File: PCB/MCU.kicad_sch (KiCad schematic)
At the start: 36 parts, among them J1 MSD-1-A, SW33V1 Conn_01x01_Pin

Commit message: Updated component selection; Updated some footprints; Added .csv file in the export folder of the PCB that contains parts from DigiKey
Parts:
- Cnrst1: footprint Capacitor_SMD:C_0603_1608Metric -> Capacitor_SMD:C_0805_2012Metric
- Csd_shield1: footprint Capacitor_SMD:C_1206_3216Metric -> Capacitor_SMD:C_0805_2012Metric
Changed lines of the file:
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@@
 			)
 		)
-		(property "Footprint" "Capacitor_SMD:C_0603_1608Metric"
+		(property "Footprint" "Capacitor_SMD:C_0805_2012Metric"
 			(at 80.5688 32.766 0)
 			(effects
@@
 			)
 		)
-		(property "Footprint" "Capacitor_SMD:C_1206_3216Metric"
+		(property "Footprint" "Capacitor_SMD:C_0805_2012Metric"
 			(at 211.836 76.5048 0)
 			(effects

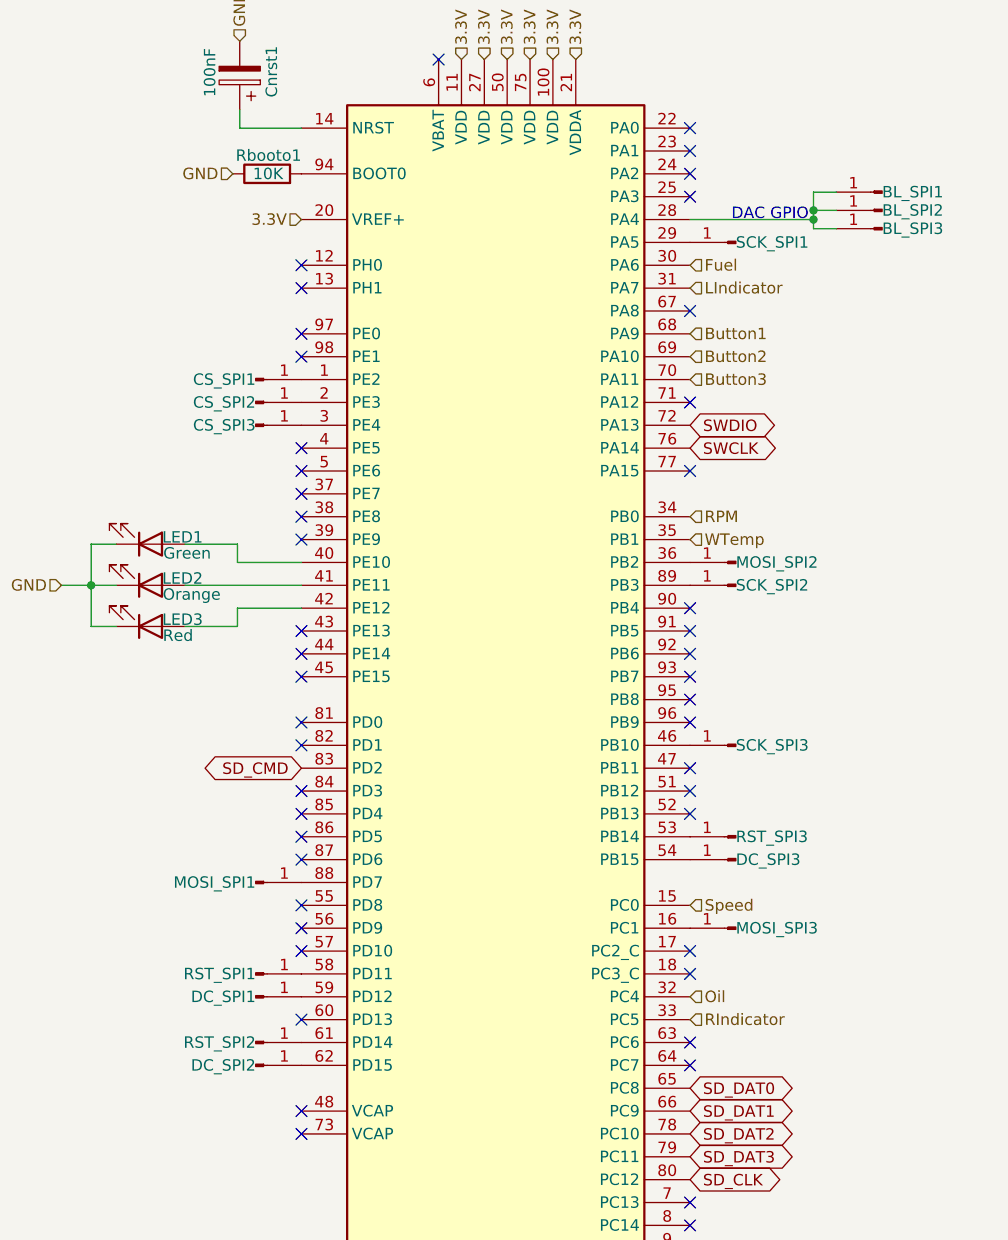
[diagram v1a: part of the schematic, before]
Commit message: Added 2x Temperature Sensors; Updated wrong GPIO connections in schematic; Set Button input GPIOs to Pull-Down; LED circuits need to be corrected
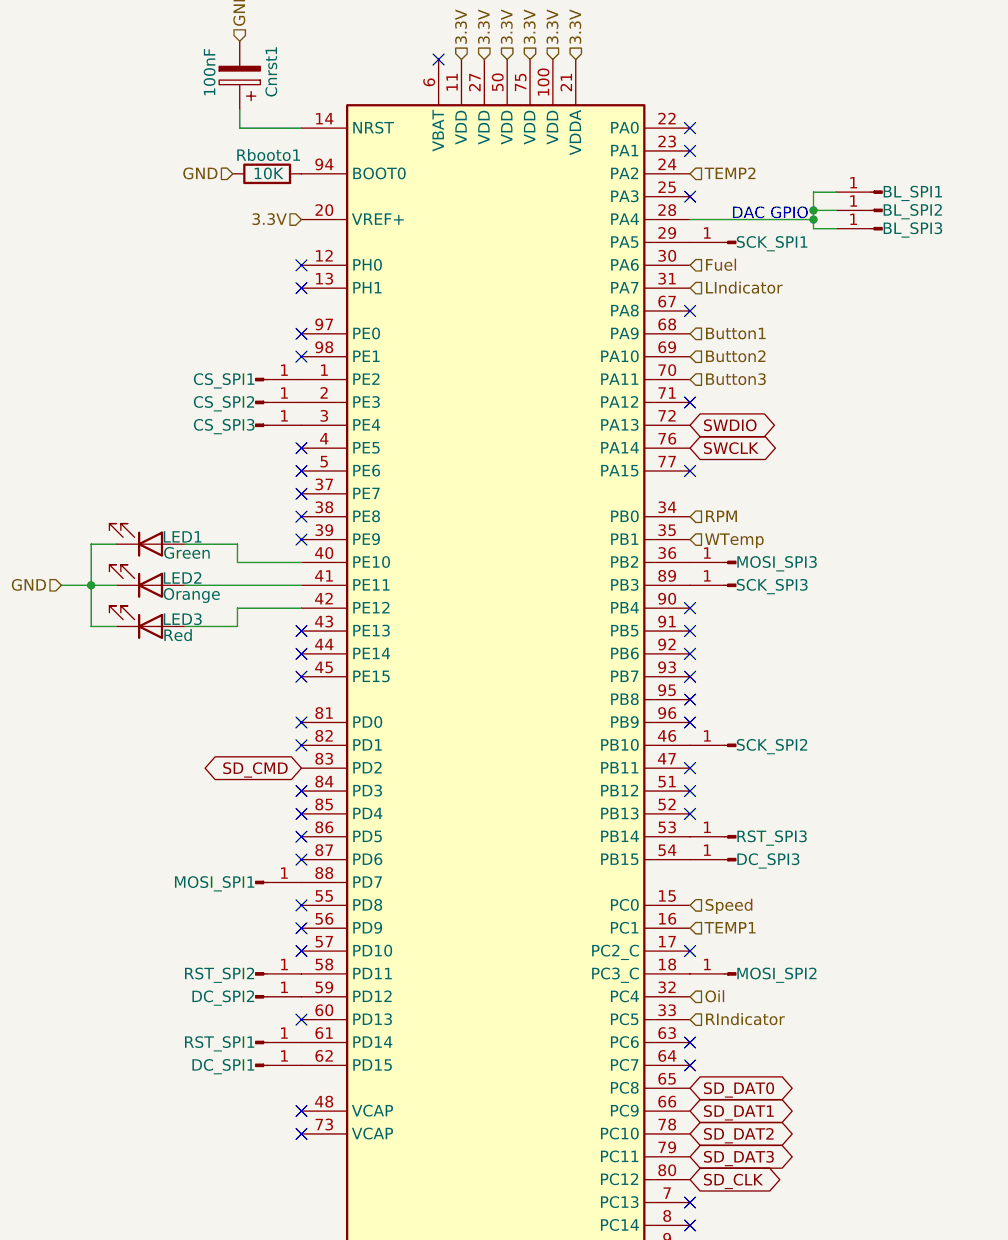
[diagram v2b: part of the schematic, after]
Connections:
- net at MOSI_SPI3.1 (Pin_1): now also STM1.36 (PB2); no longer STM1.16 (PC1)
- net at STM1.46 (PB10): now also SCK_SPI2.1 (Pin_1); no longer SCK_SPI3.1 (Pin_1)
- net at DC_SPI2.1 (Pin_1): now also STM1.59 (PD12); no longer STM1.62 (PD15)
- net at RST_SPI1.1 (Pin_1): now also STM1.61 (PD14); no longer STM1.58 (PD11)
- net at STM1.18 (PC3_C): now also MOSI_SPI2.1 (Pin_1)
- net TEMP2: now reaches STM1.24 (PA2)
- net at DC_SPI1.1 (Pin_1): now also STM1.62 (PD15); no longer STM1.59 (PD12)
- net at RST_SPI2.1 (Pin_1): now also STM1.58 (PD11); no longer STM1.61 (PD14)
- net at STM1.89 (PB3): now also SCK_SPI3.1 (Pin_1); no longer SCK_SPI2.1 (Pin_1)
- new net TEMP1: STM1.16 (PC1)
- no-connect marks 49 -> 47

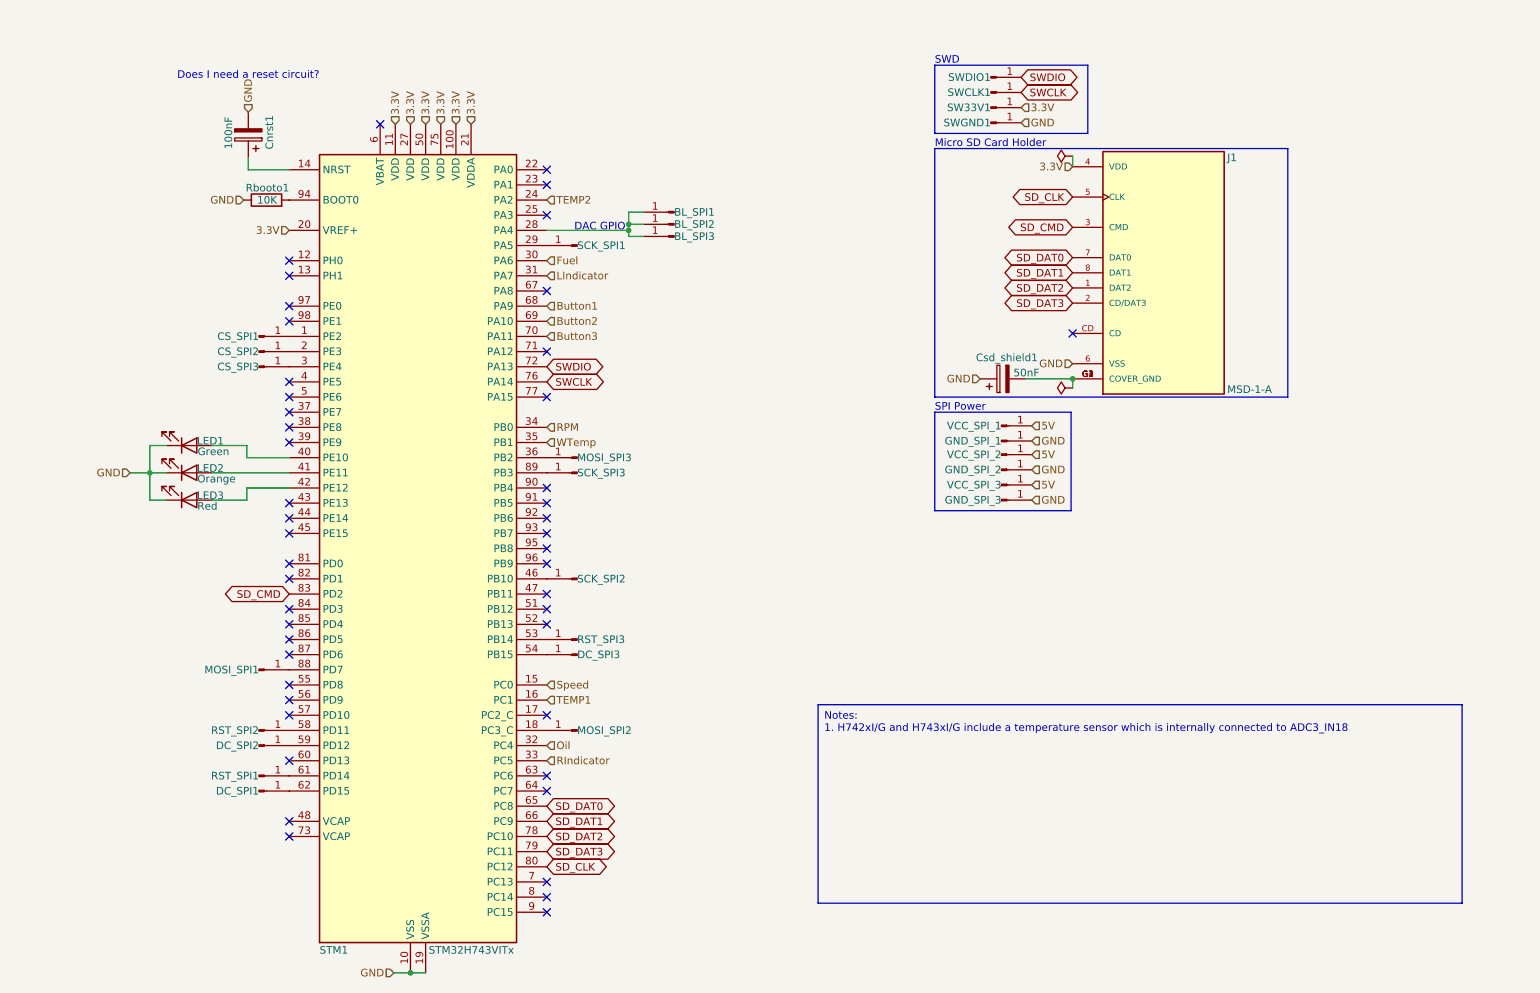
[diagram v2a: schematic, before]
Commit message: add resistors for status LEDs
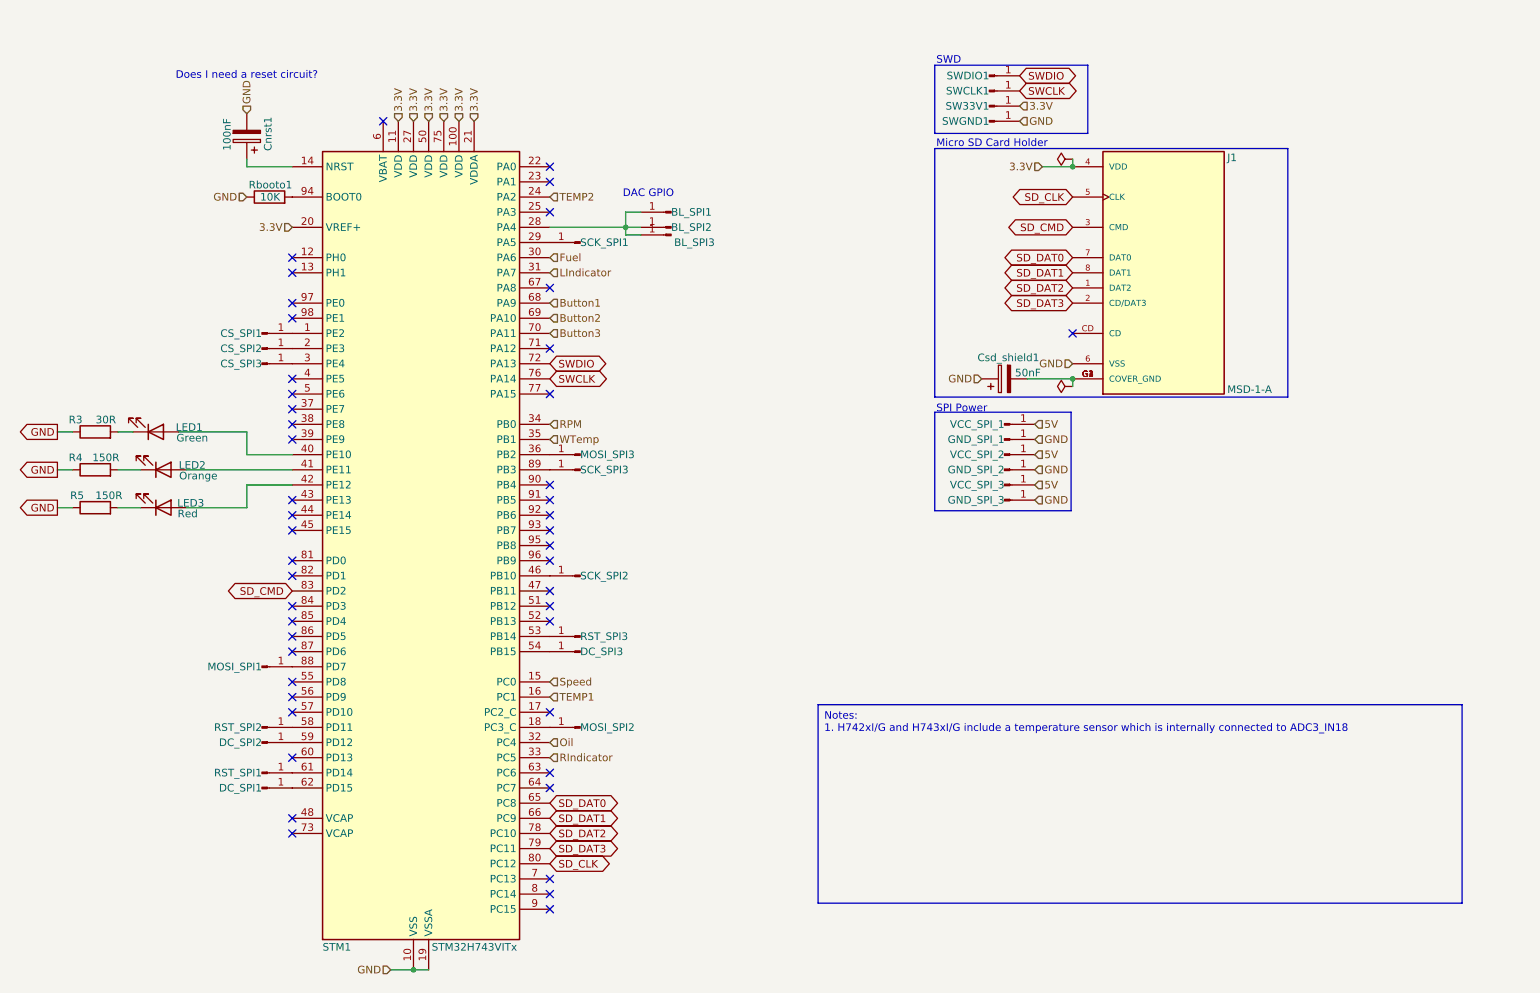
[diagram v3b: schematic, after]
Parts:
- added R3: 30R, symbol Device:R
- added R4, R5: 150R, symbol Device:R
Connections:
- net GND: now also R3.1, R4.1, R5.1; no longer LED1.1 (K), LED2.1 (K), LED3.1 (K)
- new net: LED2.1 (K), R4.2
- new net: LED1.1 (K), R3.2
- new net: LED3.1 (K), R5.2
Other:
- moved on the sheet: BL_SPI1, BL_SPI2, BL_SPI3, CS_SPI1, CS_SPI2, CS_SPI3, DC_SPI1, DC_SPI2, DC_SPI3, GND_SPI_1, GND_SPI_2, GND_SPI_3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

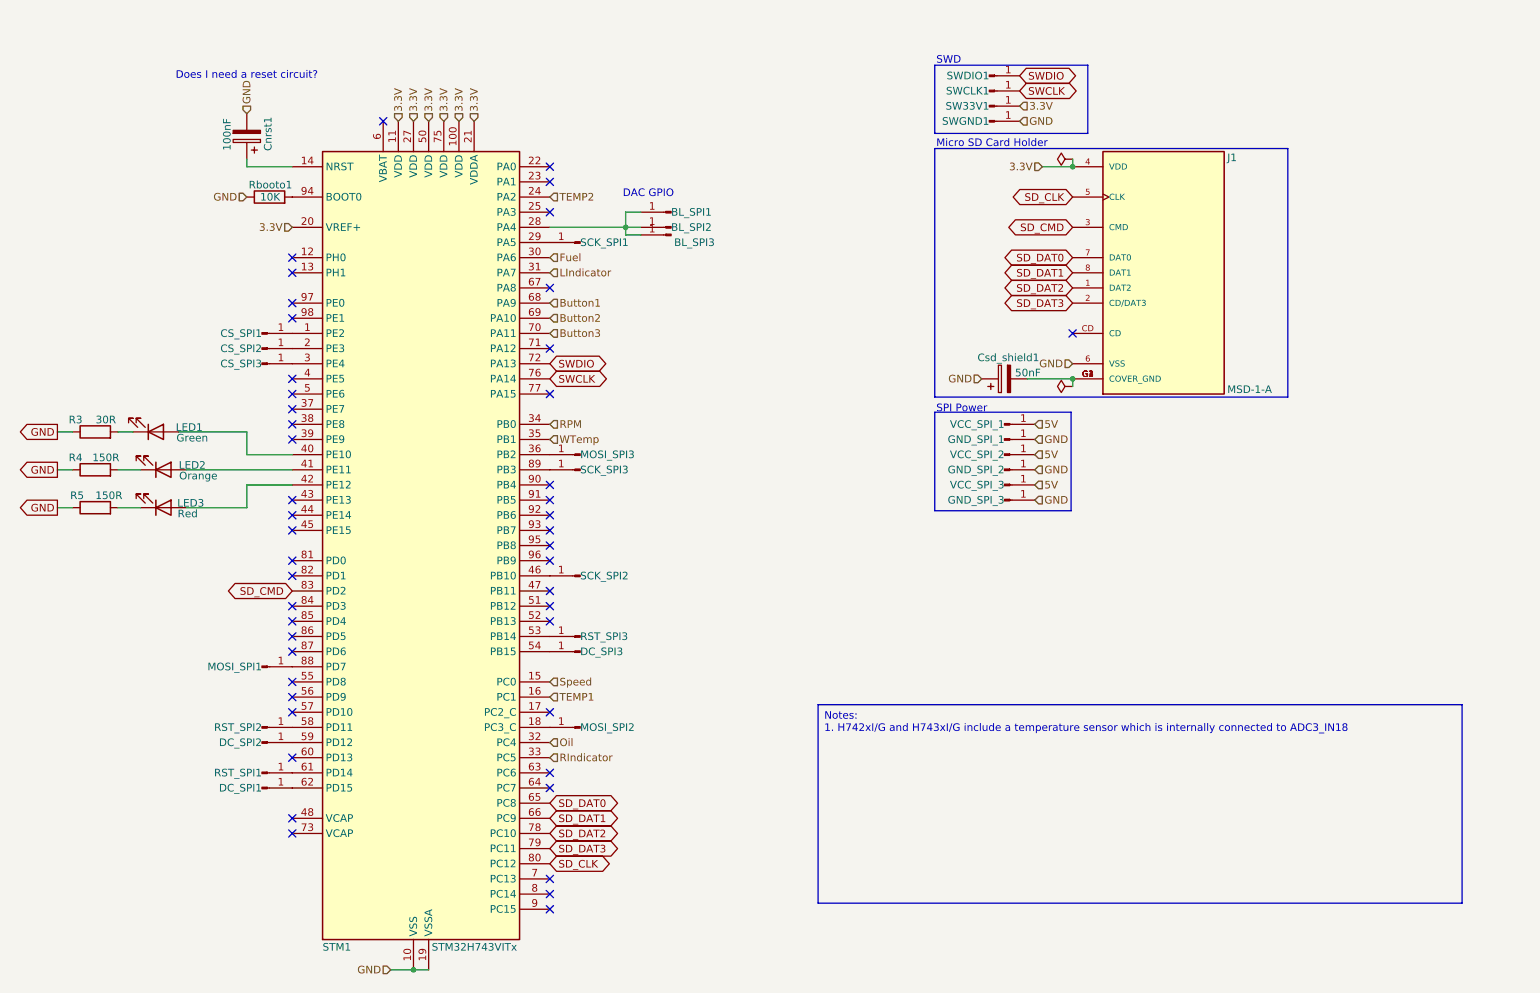
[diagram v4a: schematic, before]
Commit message: Replaced some global labels with power net(s); Added warning label for missing component
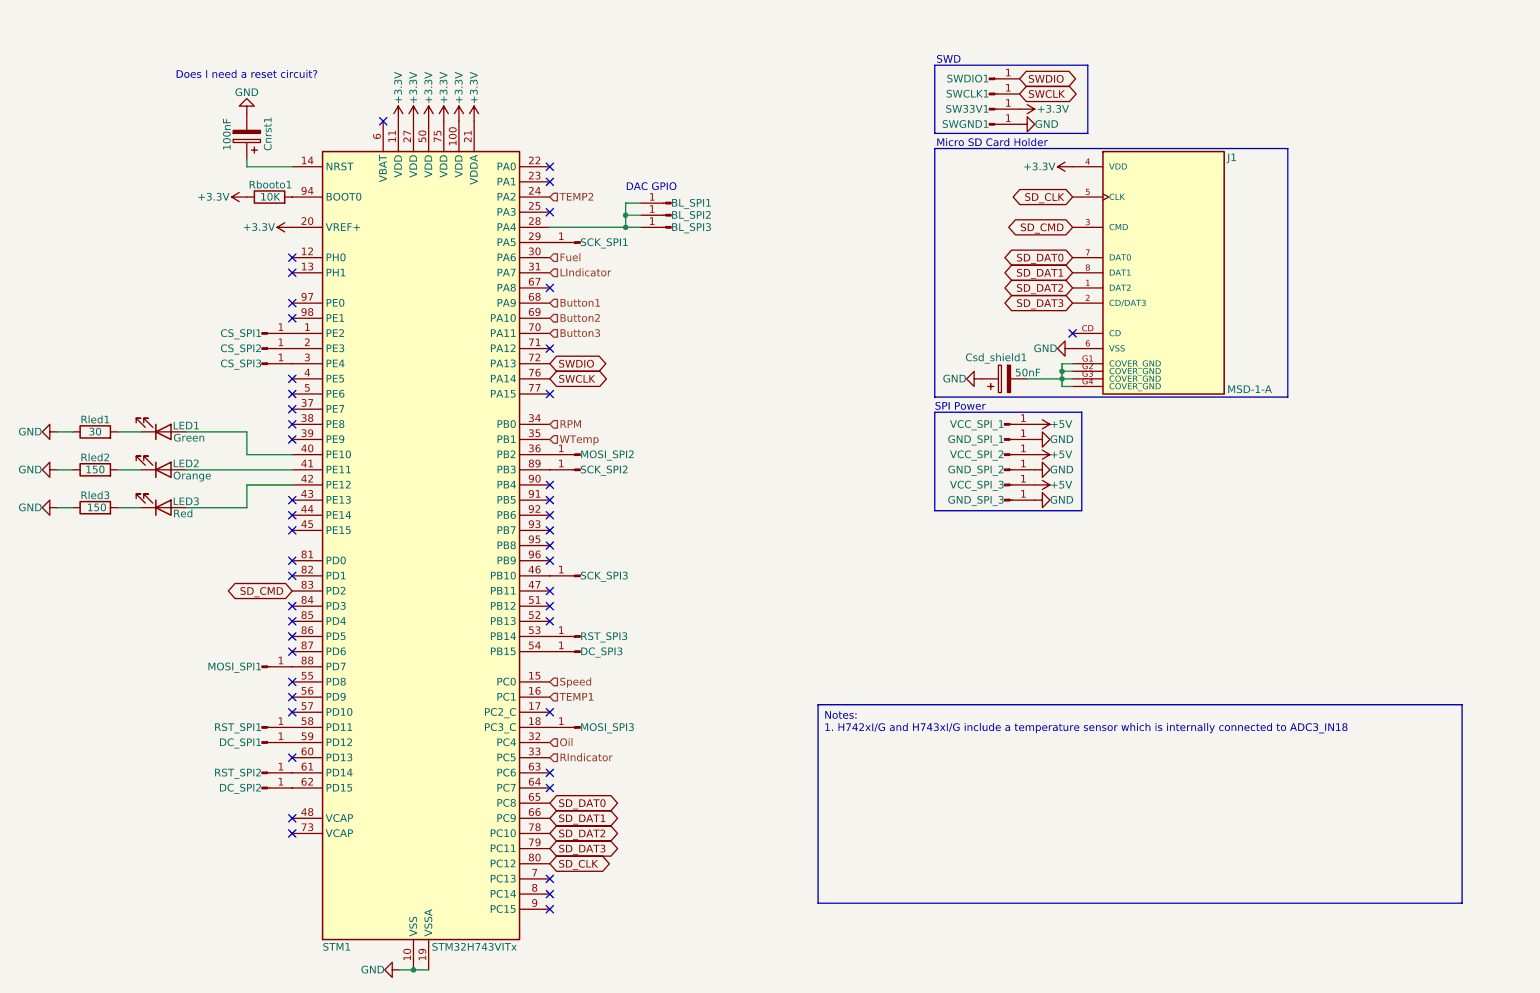
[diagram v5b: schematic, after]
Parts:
- Rled1: renamed from R3; value 30R -> 30; footprint (none) -> Resistor_SMD:R_0603_1608Metric
- Rled2: renamed from R4; value 150R -> 150; footprint (none) -> Resistor_SMD:R_0603_1608Metric
- Rled3: renamed from R5; value 150R -> 150; footprint (none) -> Resistor_SMD:R_0603_1608Metric
- renumbered DC_SPI2 to DC_SPI1, DC_SPI1 to DC_SPI2, MOSI_SPI3 to MOSI_SPI2, MOSI_SPI2 to MOSI_SPI3, RST_SPI2 to RST_SPI1, RST_SPI1 to RST_SPI2, SCK_SPI3 to SCK_SPI2, SCK_SPI2 to SCK_SPI3
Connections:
- net GND: no longer Rbooto1.1
- net 3.3V renamed +3.3V
- net +3.3V: now also Rbooto1.1
- net 5V renamed +5V
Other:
- moved on the sheet: BL_SPI1, BL_SPI2, BL_SPI3, LED1, SW33V1, SWCLK1, SWDIO1, SWGND1

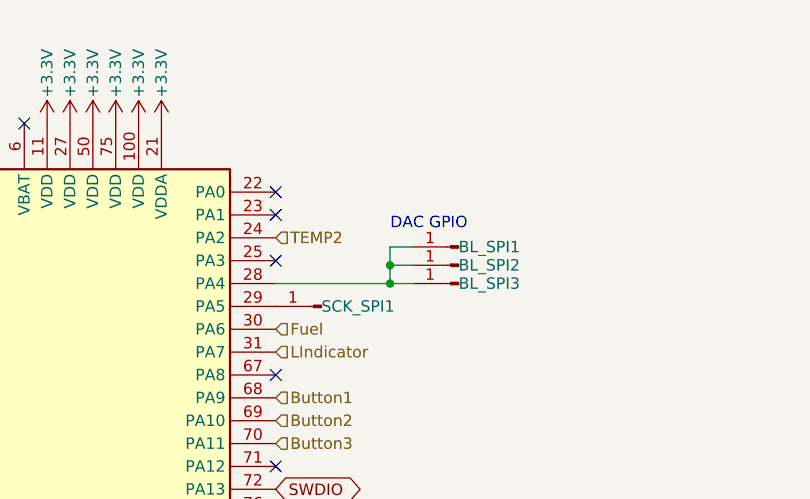
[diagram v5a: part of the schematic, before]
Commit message: Finalized circuit design; First try of PCB layout (FAILED)
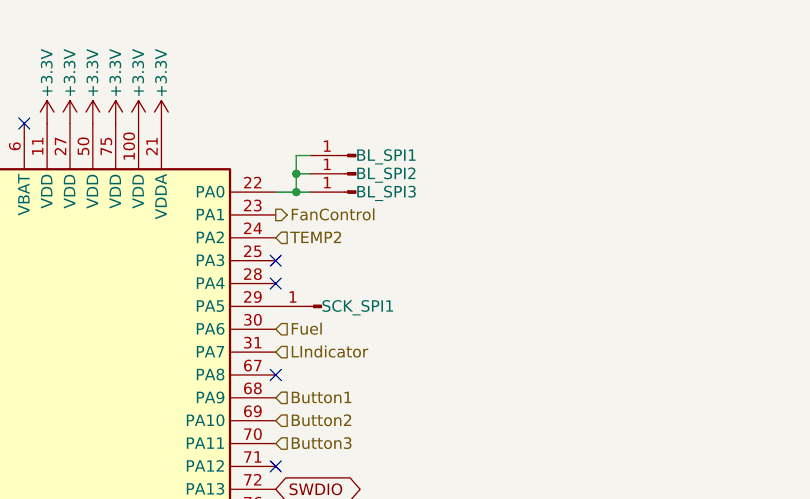
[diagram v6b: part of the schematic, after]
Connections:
- net at BL_SPI1.1 (Pin_1), BL_SPI2.1 (Pin_1), BL_SPI3.1 (Pin_1): now also STM1.22 (PA0); no longer STM1.28 (PA4)
- net FanControl: now reaches STM1.23 (PA1)
- no-connect marks 47 -> 46
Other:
- note removed: "DAC GPIO"
